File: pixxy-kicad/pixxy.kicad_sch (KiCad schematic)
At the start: 24 parts, among them Q1 2N3904, SW17 SW_SPDT, U1 Pico

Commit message: Add rev1 pcb files
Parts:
- R1: value 15R -> 10R
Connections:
- net MTX_COL2: now reaches SW10.1, SW14.1, SW2.1, SW6.1, U1.16 (GPIO12)
- net MTX_ROW1: now reaches SW1.2, SW2.2, SW3.2, SW4.2, U1.12 (GPIO9)
- net MTX_COL3: now reaches SW11.1, SW15.1, SW3.1, SW7.1, U1.15 (GPIO11)
- net MTX_ROW3: now reaches SW10.2, SW11.2, SW12.2, SW9.2, U1.10 (GPIO7)
- net MTX_COL1: now reaches SW1.1, SW13.1, SW5.1, SW9.1, U1.17 (GPIO13)
- net MTX_ROW2: now reaches SW5.2, SW6.2, SW7.2, SW8.2, U1.11 (GPIO8)
- net MTX_COL4: now reaches SW12.1, SW16.1, SW4.1, SW8.1, U1.14 (GPIO10)
- net POT_G: now reaches RV2.2, U1.32 (GPIO27_ADC1)
- net MTX_ROW4: now reaches SW13.2, SW14.2, SW15.2, SW16.2, U1.9 (GPIO6)
- net POT_B: now reaches RV3.2, U1.34 (GPIO28_ADC2)
- net SW_ONCE_REPEAT: now reaches SW17.1 (A), U1.4 (GPIO2)
- net LED_SIG: now reaches Q1.2 (B), U1.21 (GPIO16)
- net POT_R: now reaches RV1.2, U1.31 (GPIO26_ADC0)
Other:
- moved on the sheet: D1, R1, RV1, RV2, RV3, SW1, SW10, SW11, SW12, SW13, SW14, SW15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

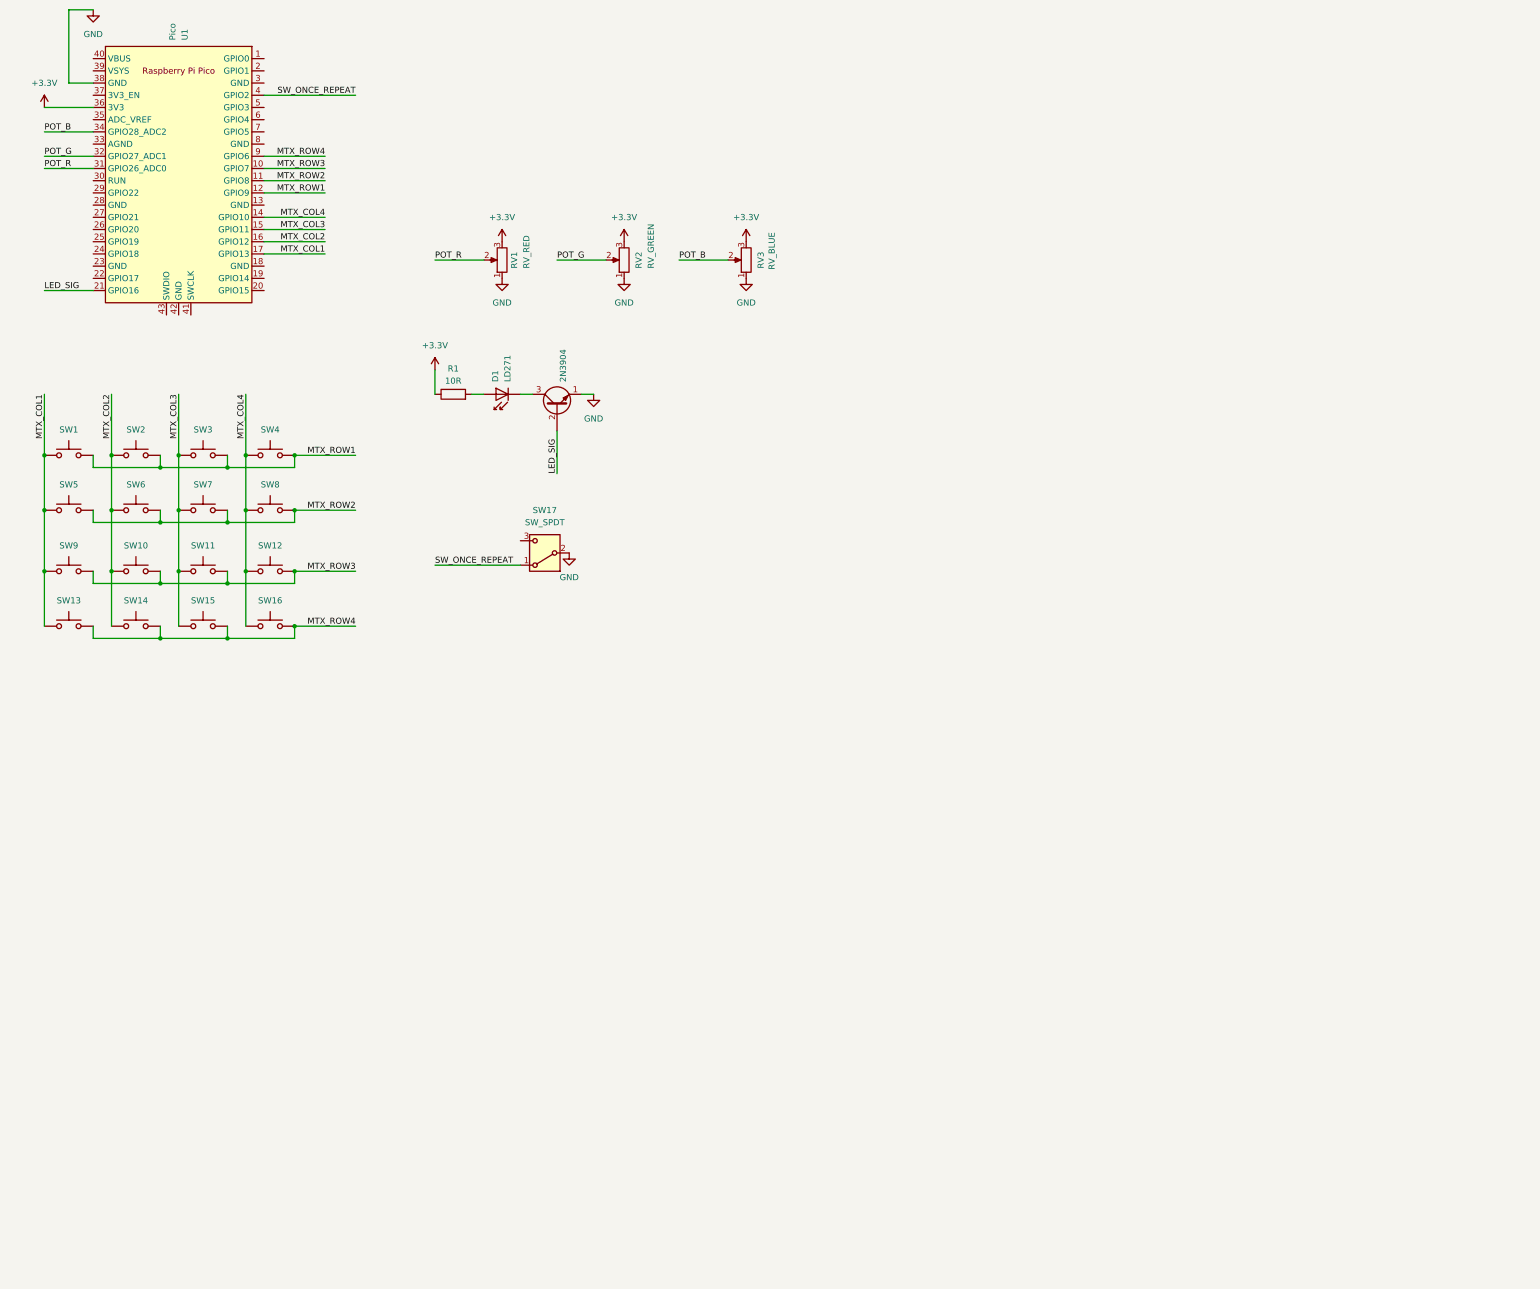
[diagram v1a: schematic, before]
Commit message: Add RP2040-based schematic
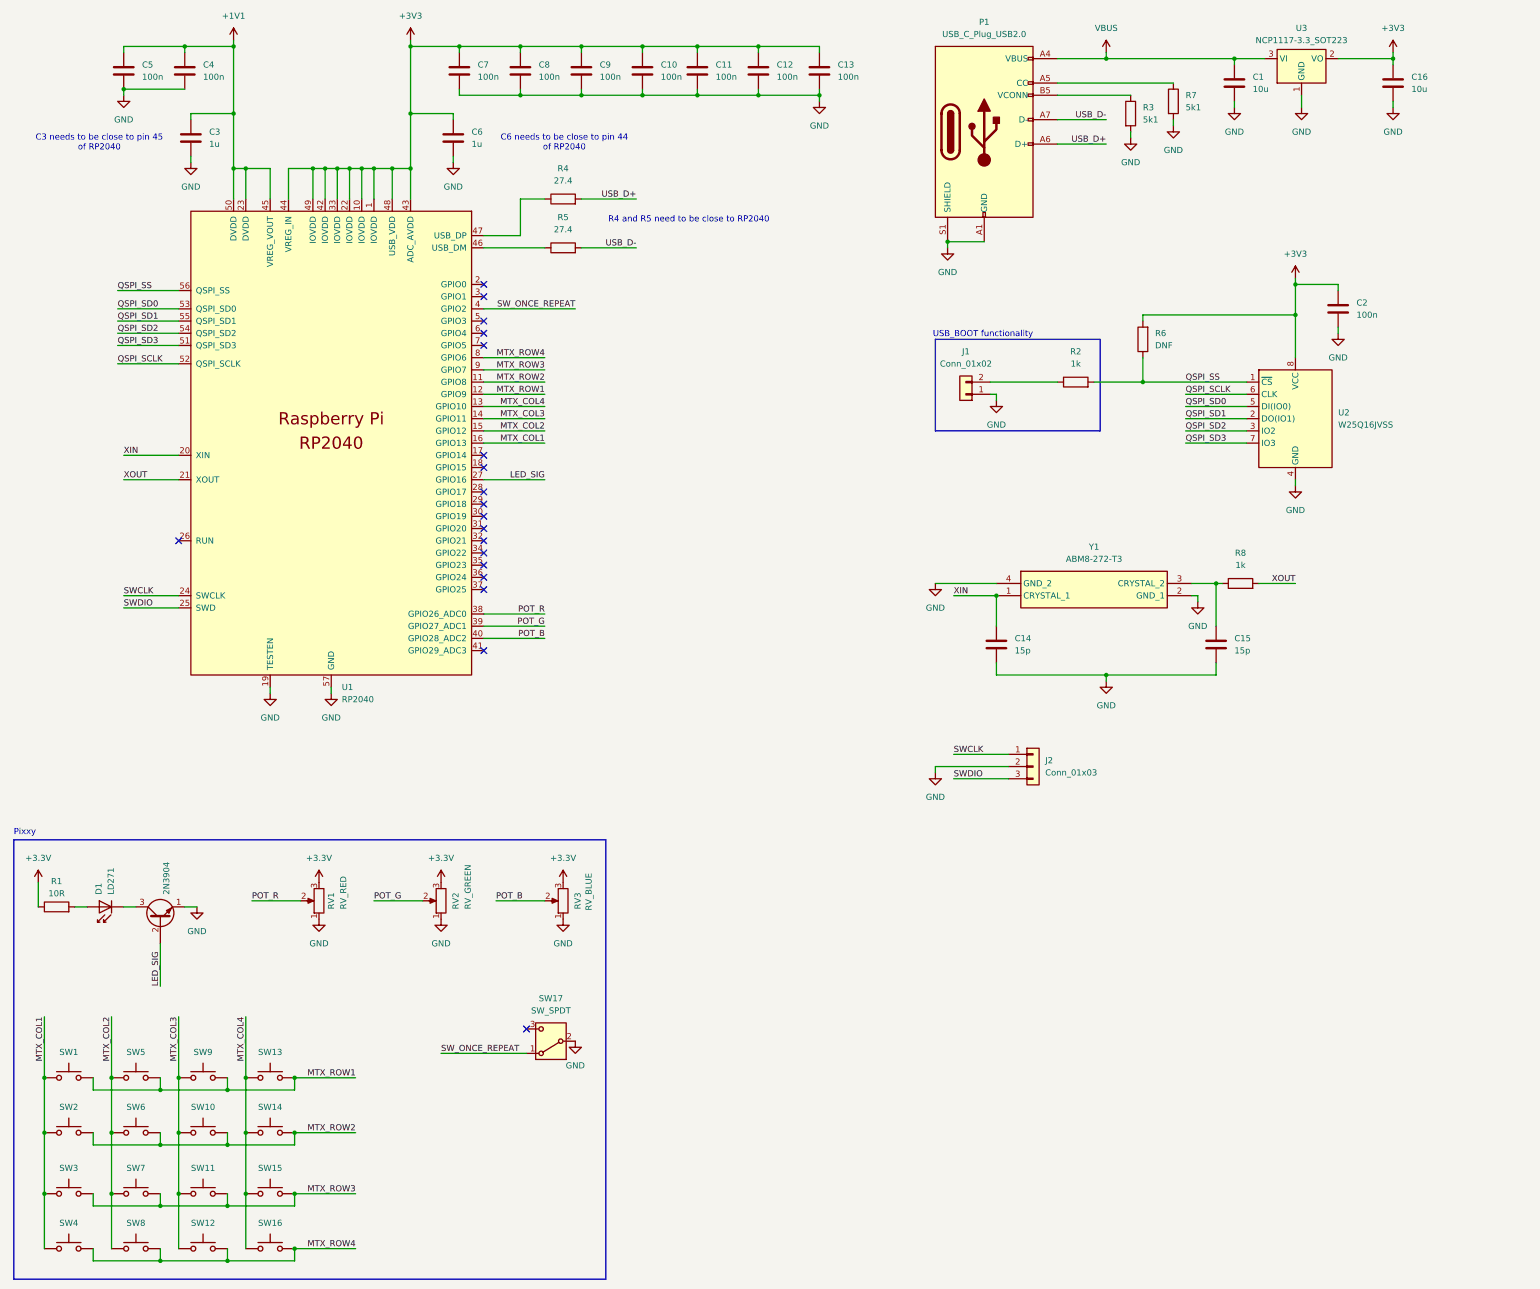
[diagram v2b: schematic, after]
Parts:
- removed U1: Pico, MCU_RaspberryPi_and_Boards:RPi_Pico_SMD, symbol MCU_RaspberryPi_and_Boards:Pico
- added C1, C16: 10u, Capacitor_SMD:C_0603_1608Metric, symbol Device:C
- added C10, C11, C12, C13, C2, C4, C5, C7, C8, C9: 100n, Capacitor_SMD:C_0402_1005Metric, symbol Device:C
- added C14, C15: 15p, Capacitor_SMD:C_0402_1005Metric, symbol Device:C
- added C3, C6: 1u, Capacitor_SMD:C_0603_1608Metric, symbol Device:C
- added J1: Conn_01x02, Connector_PinSocket_2.54mm:PinSocket_1x02_P2.54mm_Vertical, symbol Connector_Generic:Conn_01x02
- added J2: Conn_01x03, Connector_PinSocket_2.54mm:PinSocket_1x03_P2.54mm_Vertical, symbol Connector_Generic:Conn_01x03
- added P1: USB_C_Plug_USB2.0, Connector_USB:USB_C_Receptacle_G-Switch_GT-USB-7010ASV, symbol Connector:USB_C_Plug_USB2.0
- added R2, R8: 1k, Resistor_SMD:R_0402_1005Metric, symbol Device:R
- added R3, R7: 5k1, Resistor_SMD:R_0603_1608Metric, symbol Device:R
- added R4, R5: 27.4, Resistor_SMD:R_0402_1005Metric, symbol Device:R
- added R6: DNF, symbol Device:R
- added U1: RP2040, MCU_RaspberryPi_and_Boards:RP2040-QFN-56, symbol MCU_RaspberryPi_and_Boards:RP2040
- added U2: W25Q16JVSS, Package_SO:SOIC-8_5.23x5.23mm_P1.27mm, symbol Memory_Flash:W25Q16JVSS
- added U3: NCP1117-3.3_SOT223, Package_TO_SOT_SMD:SOT-223-3_TabPin2, symbol Regulator_Linear:NCP1117-3.3_SOT223
- added Y1: ABM8-272-T3, ABM8272T3, symbol SamacSys_Parts:ABM8-272-T3
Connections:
- net GND: now also C1.2, C10.2, C11.2, C12.2, C13.2, C14.2, C15.2, C16.2, C2.2, C3.2, C4.2, C5.2, C6.2, C7.2, C8.2, C9.2, J1.1 (Pin_1), J2.2 (Pin_2), P1.A1 (GND), P1.A12 (GND), P1.B1 (GND), P1.B12 (GND), P1.S1 (SHIELD), R3.2, R7.2, U1.19 (TESTEN), U1.57 (GND), U2.4 (GND), U3.1 (GND), Y1.2 (GND_1), Y1.4 (GND_2)
- net LED_SIG: now also U1.27 (GPIO16)
- net MTX_COL1: now also SW2.1, SW3.1, SW4.1, U1.16 (GPIO13); no longer SW13.1, SW5.1, SW9.1
- net MTX_COL2: now also SW5.1, SW7.1, SW8.1, U1.15 (GPIO12); no longer SW10.1, SW14.1, SW2.1
- net MTX_COL3: now also SW10.1, SW12.1, SW9.1, U1.14 (GPIO11); no longer SW15.1, SW3.1, SW7.1
- net MTX_COL4: now also SW13.1, SW14.1, SW15.1, U1.13 (GPIO10); no longer SW12.1, SW4.1, SW8.1
- net MTX_ROW1: now also SW13.2, SW5.2, SW9.2, U1.12 (GPIO9); no longer SW2.2, SW3.2, SW4.2
- net MTX_ROW2: now also SW10.2, SW14.2, SW2.2, U1.11 (GPIO8); no longer SW5.2, SW7.2, SW8.2
- net MTX_ROW3: now also SW15.2, SW3.2, SW7.2, U1.9 (GPIO7); no longer SW10.2, SW12.2, SW9.2
- net MTX_ROW4: now also SW12.2, SW4.2, SW8.2, U1.8 (GPIO6); no longer SW13.2, SW14.2, SW15.2
- net POT_B: now also U1.40 (GPIO28_ADC2)
- net POT_G: now also U1.39 (GPIO27_ADC1)
- net POT_R: now also U1.38 (GPIO26_ADC0)
- net SW_ONCE_REPEAT: now also U1.4 (GPIO2)
- new net: R5.1, U1.46 (USB_DM)
- new net: R4.1, U1.47 (USB_DP)
- new net: P1.B5 (VCONN), R3.1
- new net: J1.2 (Pin_2), R2.1
- new net: P1.A5 (CC), R7.1
- new net: C15.1, R8.1, Y1.3 (CRYSTAL_2)
- new net +1V1: C3.1, C4.1, C5.1, U1.23 (DVDD), U1.45 (VREG_VOUT), U1.50 (DVDD)
- new net +3V3: C10.1, C11.1, C12.1, C13.1, C16.1, C2.1, C6.1, C7.1, C8.1, C9.1, R6.2, U1.1 (IOVDD), U1.10 (IOVDD), U1.22 (IOVDD), U1.33 (IOVDD), U1.42 (IOVDD), U1.43 (ADC_AVDD), U1.44 (VREG_IN), U1.48 (USB_VDD), U1.49 (IOVDD), U2.8 (VCC), U3.2 (VO)
- new net QSPI_SCLK: U1.52 (QSPI_SCLK), U2.6 (CLK)
- new net QSPI_SD0: U1.53 (QSPI_SD0), U2.5 (DI(IO0))
- new net QSPI_SD1: U1.55 (QSPI_SD1), U2.2 (DO(IO1))
- new net QSPI_SD2: U1.54 (QSPI_SD2), U2.3 (IO2)
- new net QSPI_SD3: U1.51 (QSPI_SD3), U2.7 (IO3)
- new net QSPI_SS: R2.2, R6.1, U1.56 (QSPI_SS), U2.1 (~{CS})
- new net SWCLK: J2.1 (Pin_1), U1.24 (SWCLK)
- new net SWDIO: J2.3 (Pin_3), U1.25 (SWD)
- new net USB_D+: P1.A6 (D+), R4.2
- new net USB_D-: P1.A7 (D-), R5.2
- new net VBUS: C1.1, P1.A4 (VBUS), P1.A9 (VBUS), P1.B4 (VBUS), P1.B9 (VBUS), U3.3 (VI)
- new net XIN: C14.1, U1.20 (XIN), Y1.1 (CRYSTAL_1)
- new net XOUT: R8.2, U1.21 (XOUT)
- no-connect marks 0 -> 19
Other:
- note added: "C3 needs to be close to pin 45 of RP2040"
- note added: "C6 needs to be close to pin 44 of RP2040"
- note added: "Pixxy"
- note added: "R4 and R5 need to be close to RP2040"
- note added: "USB_BOOT functionality"
- moved on the sheet: RV1, RV2, RV3

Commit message: Improved schematic and finished pcb for rev2
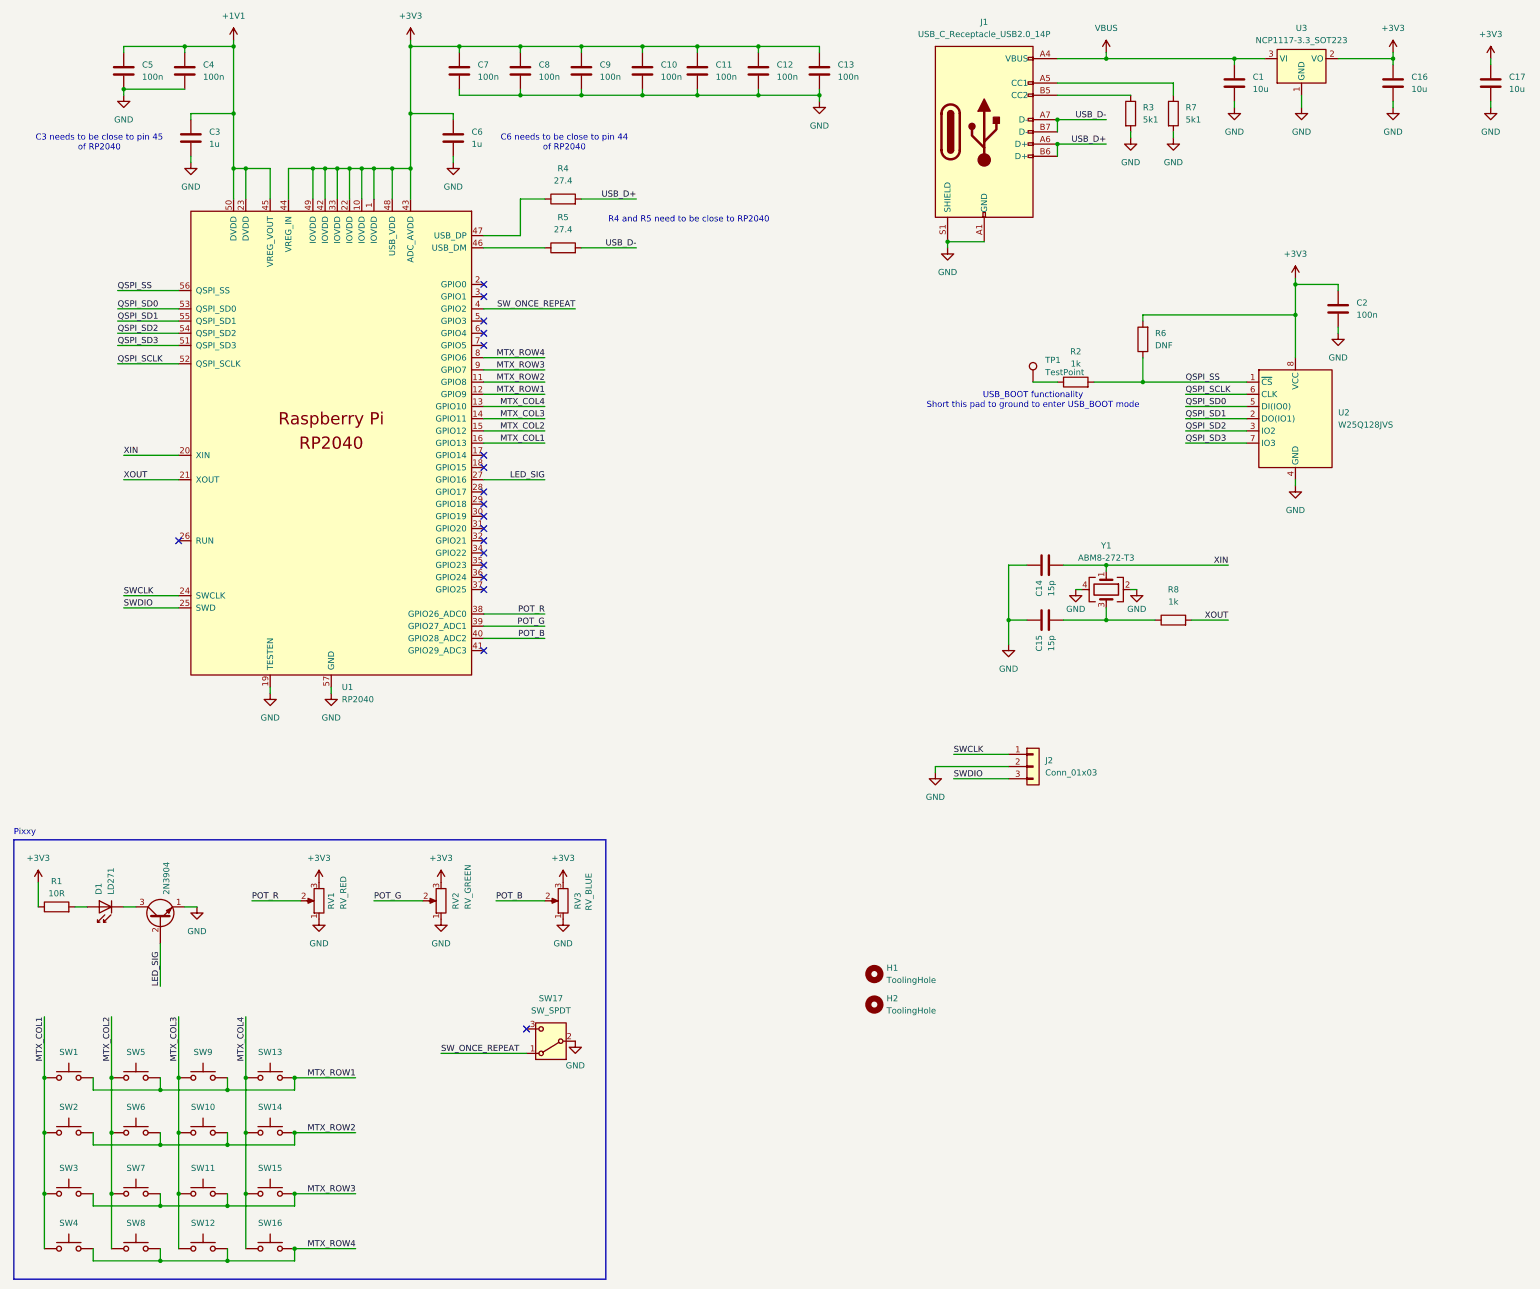
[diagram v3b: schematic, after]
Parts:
- removed J1: Conn_01x02, Connector_PinSocket_2.54mm:PinSocket_1x02_P2.54mm_Vertical, symbol Connector_Generic:Conn_01x02
- removed P1: USB_C_Plug_USB2.0, Connector_USB:USB_C_Receptacle_G-Switch_GT-USB-7010ASV, symbol Connector:USB_C_Plug_USB2.0
- removed Y1: ABM8-272-T3, ABM8272T3, symbol SamacSys_Parts:ABM8-272-T3
- added C17: 10u, Capacitor_SMD:C_0805_2012Metric, symbol Device:C
- added H1, H2: ToolingHole, MountingHole:MountingHole_1.152mm, symbol Mechanical:MountingHole
- added J1: USB_C_Receptacle_USB2.0_14P, Connector_USB:USB_C_Receptacle_G-Switch_GT-USB-7010ASV, symbol Connector:USB_C_Receptacle_USB2.0_14P
- added TP1: TestPoint, TestPoint:TestPoint_Pad_1.5x1.5mm, symbol Connector:TestPoint
- added Y1: ABM8-272-T3, Crystal:Crystal_SMD_3225-4Pin_3.2x2.5mm, symbol Device:Crystal_GND24
- C1, C16: footprint Capacitor_SMD:C_0603_1608Metric -> Capacitor_SMD:C_0805_2012Metric; LCSC C1691 -> C15850
- C10, C11, C12, C13, C2, C4, C5, C7, C8, C9: LCSC C5448791 -> C307331
- C14: LCSC (none) -> C1548
- C15: LCSC C525200 -> C1548
- C3, C6: footprint Capacitor_SMD:C_0603_1608Metric -> Capacitor_SMD:C_0402_1005Metric; LCSC C106858 -> C52923
- J2: footprint Connector_PinSocket_2.54mm:PinSocket_1x03_P2.54mm_Vertical -> Connector_JST:JST_SH_SM03B-SRSS-TB_1x03-1MP_P1.00mm_Horizontal
- R2, R8: LCSC C851604 -> C11702
- R3, R7: footprint Resistor_SMD:R_0603_1608Metric -> Resistor_SMD:R_0402_1005Metric; LCSC C105580 -> C25905
- R6: footprint (none) -> Resistor_SMD:R_0402_1005Metric
- U1: footprint MCU_RaspberryPi_and_Boards:RP2040-QFN-56 -> Package_DFN_QFN:QFN-56-1EP_7x7mm_P0.4mm_EP3.2x3.2mm; LCSC (none) -> C2040
- U2: value W25Q16JVSS -> W25Q128JVS; LCSC C82317 -> C97521
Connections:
- net +3.3V is gone; now on net +3V3: R1.1, RV1.3, RV2.3, RV3.3
- net +3V3: now also C17.1
- net GND: now also C14.1, C15.1, C17.2, J1.A1 (GND), J1.A12 (GND), J1.B1 (GND), J1.B12 (GND), J1.S1 (SHIELD), Y1.2, Y1.4; no longer C14.2, C15.2
- net USB_D+: now also J1.A6 (D+), J1.B6 (D+)
- net USB_D-: now also J1.A7 (D-), J1.B7 (D-)
- net VBUS: now also J1.A4 (VBUS), J1.A9 (VBUS), J1.B4 (VBUS), J1.B9 (VBUS)
- net XIN: now also C14.2, Y1.1; no longer C14.1
- net at R3.1: now also J1.B5 (CC2)
- net at R2.1: now also TP1.1
- net at R7.1: now also J1.A5 (CC1)
- net at R8.1: now also C15.2, Y1.3; no longer C15.1
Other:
- note added: "USB_BOOT functionality Short this pad to ground to enter USB_BOOT mode"
- note removed: "USB_BOOT functionality"
- moved on the sheet: R7
